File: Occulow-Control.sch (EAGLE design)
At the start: 39 parts, among them J1 CORTEX_DEBUG_PTH, T1 DMP3010LK3, T2 DMP3010LK3, T3 DMP3010LK3

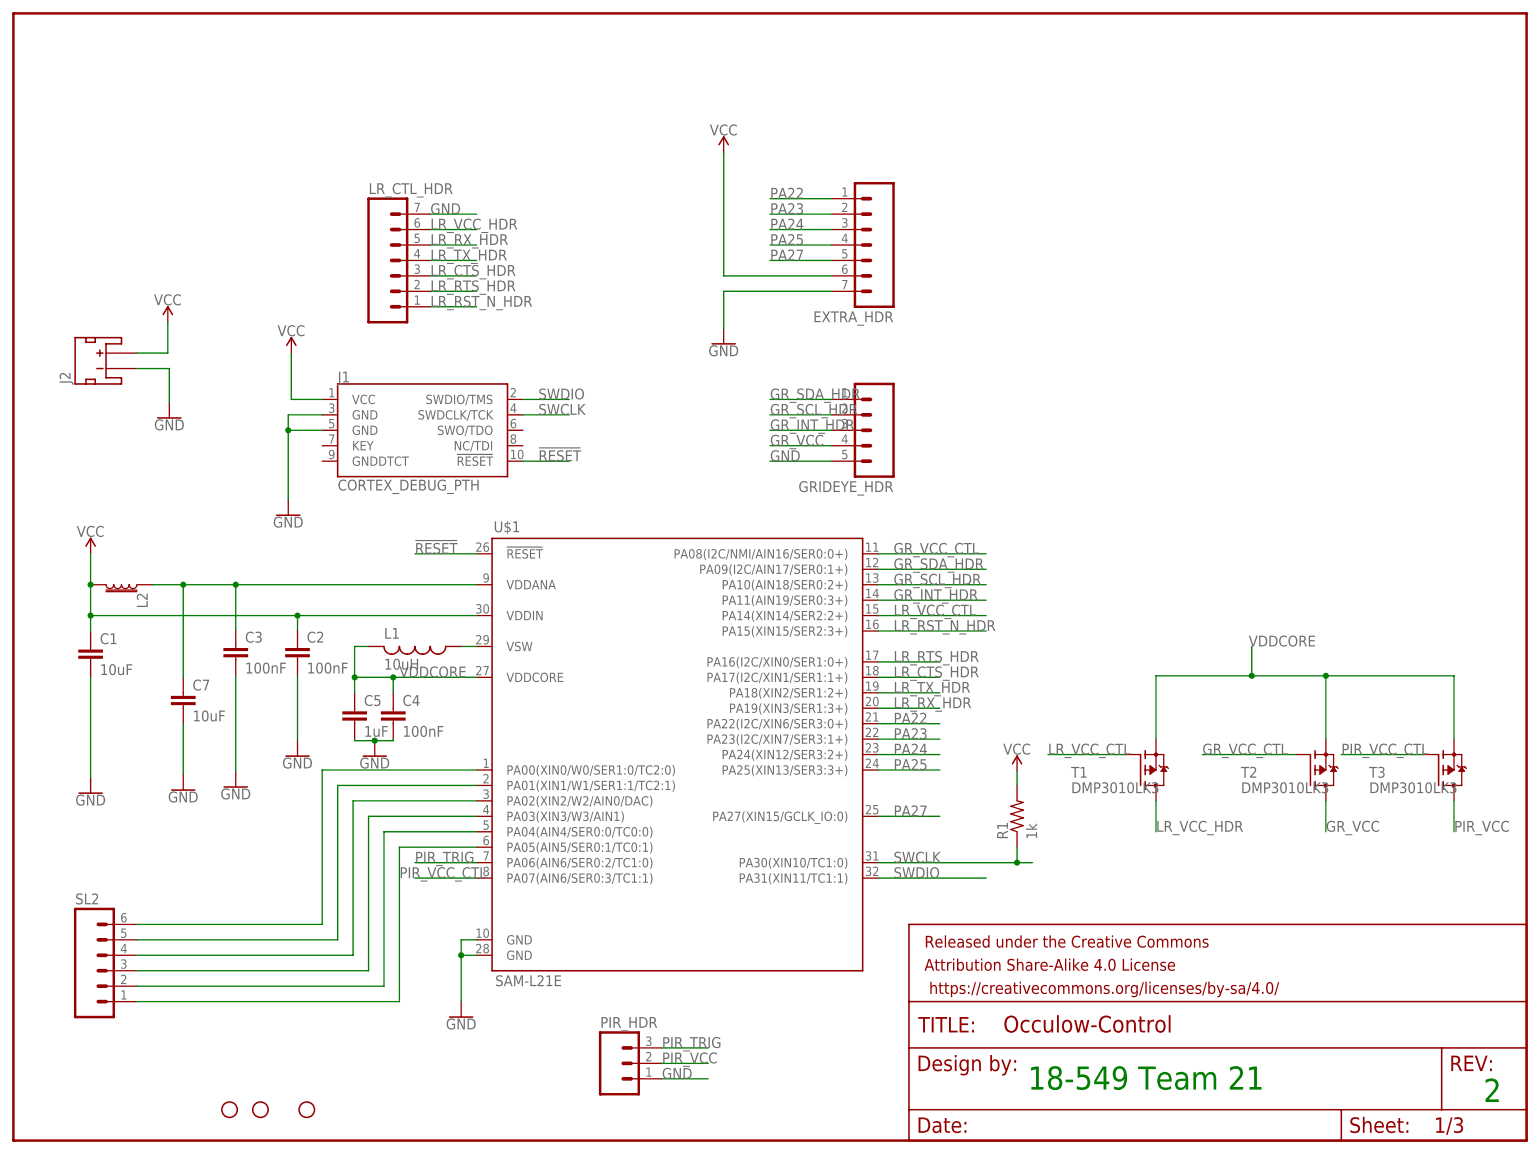
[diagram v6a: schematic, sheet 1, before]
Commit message: SAM portion fully routed
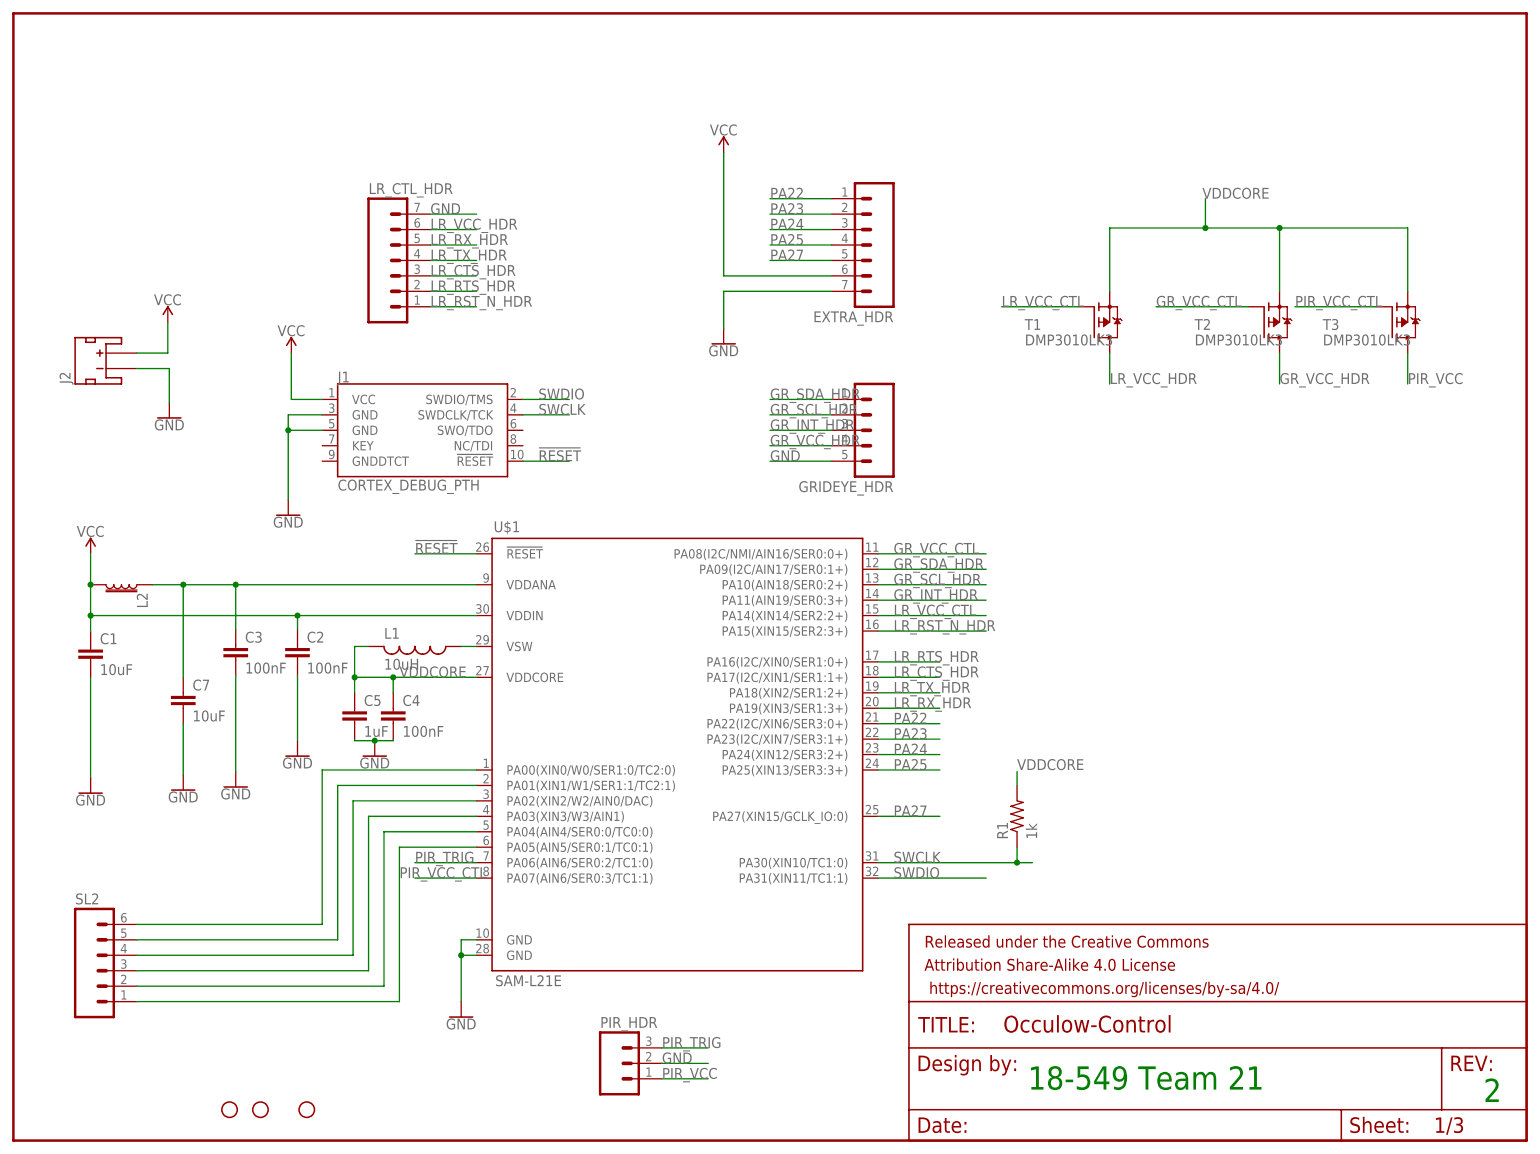
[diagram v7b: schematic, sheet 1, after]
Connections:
- new net GR_VCC_HDR: GRIDEYE_HDR.4, T2.D
- net GND: now also PIR_HDR.2; no longer PIR_HDR.1
- net GR_VCC: no longer GRIDEYE_HDR.4, T2.D
- net PIR_VCC: now also PIR_HDR.1; no longer PIR_HDR.2
- net VCC: no longer R1.2
- net VDDCORE: now also R1.2
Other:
- moved on the sheet: T1, T2, T3
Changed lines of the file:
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@@
 <part name="T3" library="transistor-fet" deviceset="SPD30P06P" device="TO252" value="DMP3010LK3"/>
 <part name="R1" library="resistor" deviceset="R-US_" device="R1206" value="1k"/>
-<part name="SUPPLY2" library="SparkFun-PowerSymbols" deviceset="VCC" device=""/>
 <part name="J1" library="SparkFun-Connectors" deviceset="CORTEX_DEBUG" device="_PTH"/>
 <part name="SUPPLY4" library="SparkFun-PowerSymbols" deviceset="VCC" device=""/>
@@
 <instance part="GND2" gate="1" x="12.7" y="57.15"/>
 <instance part="GND3" gate="1" x="36.576" y="58.166"/>
-<instance part="T1" gate="G$1" x="185.42" y="60.96"/>
+<instance part="T1" gate="G$1" x="177.8" y="134.62"/>
 <instance part="GRIDEYE_HDR" gate="G$1" x="142.24" y="116.84" rot="R180"/>
-<instance part="T2" gate="G$1" x="213.36" y="60.96"/>
+<instance part="T2" gate="G$1" x="205.74" y="134.62"/>
 <instance part="PIR_HDR" gate="G$1" x="99.06" y="12.7"/>
-<instance part="T3" gate="G$1" x="234.442" y="60.96"/>
+<instance part="T3" gate="G$1" x="226.822" y="134.62"/>
 <instance part="R1" gate="G$1" x="165.1" y="53.34" rot="R90"/>
-<instance part="SUPPLY2" gate="G$1" x="165.1" y="60.706"/>
 <instance part="J1" gate="G$1" x="66.04" y="116.84"/>
 <instance part="SUPPLY4" gate="G$1" x="45.72" y="129.54"/>
@@
 </segment>
 <segment>
-<pinref part="PIR_HDR" gate="G$1" pin="1"/>
-<wire x1="106.68" y1="10.16" x2="114.3" y2="10.16" width="0.1524" layer="91"/>
-<label x="106.68" y="10.16" size="1.778" layer="95"/>
+<pinref part="PIR_HDR" gate="G$1" pin="2"/>
+<wire x1="106.68" y1="12.7" x2="114.3" y2="12.7" width="0.1524" layer="91"/>
+<label x="106.68" y="12.7" size="1.778" layer="95"/>
 </segment>
 <segment>
@@
 </net>
 <net name="VCC" class="0">
-<segment>
-<pinref part="SUPPLY2" gate="G$1" pin="VCC"/>
-<pinref part="R1" gate="G$1" pin="2"/>
-<wire x1="165.1" y1="60.706" x2="165.1" y2="58.42" width="0.1524" layer="91"/>
-</segment>
 <segment>
 <pinref part="J1" gate="G$1" pin="VCC"/>
@@
 <segment>
 <pinref part="T1" gate="G$1" pin="G"/>
-<wire x1="182.88" y1="63.5" x2="170.18" y2="63.5" width="0.1524" layer="91"/>
-<label x="170.18" y="63.5" size="1.778" layer="95"/>
+<wire x1="175.26" y1="137.16" x2="162.56" y2="137.16" width="0.1524" layer="91"/>
+<label x="162.56" y="137.16" size="1.778" layer="95"/>
 </segment>
 <segment>
@@
 <segment>
 <pinref part="T2" gate="G$1" pin="G"/>
-<wire x1="210.82" y1="63.5" x2="195.58" y2="63.5" width="0.1524" layer="91"/>
-<label x="195.58" y="63.5" size="1.778" layer="95"/>
+<wire x1="203.2" y1="137.16" x2="187.96" y2="137.16" width="0.1524" layer="91"/>
+<label x="187.96" y="137.16" size="1.778" layer="95"/>
 </segment>
 <segment>
@@
 <wire x1="142.24" y1="96.52" x2="160.02" y2="96.52" width="0.1524" layer="91"/>
 <label x="144.78" y="96.52" size="1.778" layer="95"/>
-</segment>
-</net>
-<net name="GR_VCC" class="0">
-<segment>
-<pinref part="T2" gate="G$1" pin="D"/>
-<wire x1="215.9" y1="55.88" x2="215.9" y2="50.8" width="0.1524" layer="91"/>
-<label x="215.9" y="50.8" size="1.778" layer="95"/>
-</segment>
-<segment>
-<pinref part="GRIDEYE_HDR" gate="G$1" pin="4"/>
-<wire x1="134.62" y1="114.3" x2="124.46" y2="114.3" width="0.1524" layer="91"/>
-<label x="124.46" y="114.3" size="1.778" layer="95"/>
 </segment>
 </net>
@@
 <net name="PIR_VCC" class="0">
 <segment>
-<pinref part="PIR_HDR" gate="G$1" pin="2"/>
-<wire x1="106.68" y1="12.7" x2="114.3" y2="12.7" width="0.1524" layer="91"/>
-<label x="106.68" y="12.7" size="1.778" layer="95"/>
+<pinref part="PIR_HDR" gate="G$1" pin="1"/>
+<wire x1="106.68" y1="10.16" x2="114.3" y2="10.16" width="0.1524" layer="91"/>
+<label x="106.68" y="10.16" size="1.778" layer="95"/>
 </segment>
 <segment>
 <pinref part="T3" gate="G$1" pin="D"/>
-<wire x1="236.982" y1="55.88" x2="236.982" y2="50.8" width="0.1524" layer="91"/>
-<label x="236.982" y="50.8" size="1.778" layer="95"/>
+<wire x1="229.362" y1="129.54" x2="229.362" y2="124.46" width="0.1524" layer="91"/>
+<label x="229.362" y="124.46" size="1.778" layer="95"/>
 </segment>
 </net>
@@
 <segment>
 <pinref part="T3" gate="G$1" pin="G"/>
-<wire x1="231.902" y1="63.5" x2="218.44" y2="63.5" width="0.1524" layer="91"/>
-<label x="218.44" y="63.5" size="1.778" layer="95"/>
+<wire x1="224.282" y1="137.16" x2="210.82" y2="137.16" width="0.1524" layer="91"/>
+<label x="210.82" y="137.16" size="1.778" layer="95"/>
 </segment>
 <segment>
@@
 </segment>
 <segment>
-<wire x1="203.708" y1="81.28" x2="203.708" y2="76.454" width="0.1524" layer="91"/>
+<wire x1="196.088" y1="154.94" x2="196.088" y2="150.114" width="0.1524" layer="91"/>
 <pinref part="T1" gate="G$1" pin="S"/>
-<wire x1="203.708" y1="76.454" x2="187.96" y2="76.454" width="0.1524" layer="91"/>
-<wire x1="187.96" y1="76.454" x2="187.96" y2="66.04" width="0.1524" layer="91"/>
+<wire x1="196.088" y1="150.114" x2="180.34" y2="150.114" width="0.1524" layer="91"/>
+<wire x1="180.34" y1="150.114" x2="180.34" y2="139.7" width="0.1524" layer="91"/>
 <pinref part="T2" gate="G$1" pin="S"/>
-<wire x1="203.708" y1="76.454" x2="215.9" y2="76.454" width="0.1524" layer="91"/>
-<wire x1="215.9" y1="76.454" x2="215.9" y2="66.04" width="0.1524" layer="91"/>
-<junction x="203.708" y="76.454"/>
+<wire x1="196.088" y1="150.114" x2="208.28" y2="150.114" width="0.1524" layer="91"/>
+<wire x1="208.28" y1="150.114" x2="208.28" y2="139.7" width="0.1524" layer="91"/>
+<junction x="196.088" y="150.114"/>
 <pinref part="T3" gate="G$1" pin="S"/>
-<wire x1="215.9" y1="76.454" x2="236.982" y2="76.454" width="0.1524" layer="91"/>
-<wire x1="236.982" y1="76.454" x2="236.982" y2="66.04" width="0.1524" layer="91"/>
-<junction x="215.9" y="76.454"/>
-<label x="203.2" y="81.28" size="1.778" layer="95"/>
+<wire x1="208.28" y1="150.114" x2="229.362" y2="150.114" width="0.1524" layer="91"/>
+<wire x1="229.362" y1="150.114" x2="229.362" y2="139.7" width="0.1524" layer="91"/>
+<junction x="208.28" y="150.114"/>
+<label x="195.58" y="154.94" size="1.778" layer="95"/>
+</segment>
+<segment>
+<pinref part="R1" gate="G$1" pin="2"/>
+<wire x1="165.1" y1="60.706" x2="165.1" y2="58.42" width="0.1524" layer="91"/>
+<label x="165.1" y="60.96" size="1.778" layer="95"/>
 </segment>
 </net>
@@
 <segment>
 <pinref part="T1" gate="G$1" pin="D"/>
-<wire x1="187.96" y1="55.88" x2="187.96" y2="50.8" width="0.1524" layer="91"/>
-<label x="187.96" y="50.8" size="1.778" layer="95"/>
+<wire x1="180.34" y1="129.54" x2="180.34" y2="124.46" width="0.1524" layer="91"/>
+<label x="180.34" y="124.46" size="1.778" layer="95"/>
 </segment>
 <segment>
@@
 </segment>
 </net>
+<net name="GR_VCC_HDR" class="0">
+<segment>
+<pinref part="GRIDEYE_HDR" gate="G$1" pin="4"/>
+<wire x1="134.62" y1="114.3" x2="124.46" y2="114.3" width="0.1524" layer="91"/>
+<label x="124.46" y="114.3" size="1.778" layer="95"/>
+</segment>
+<segment>
+<pinref part="T2" gate="G$1" pin="D"/>
+<wire x1="208.28" y1="129.54" x2="208.28" y2="124.46" width="0.1524" layer="91"/>
+<label x="208.28" y="124.46" size="1.778" layer="95"/>
+</segment>
+</net>

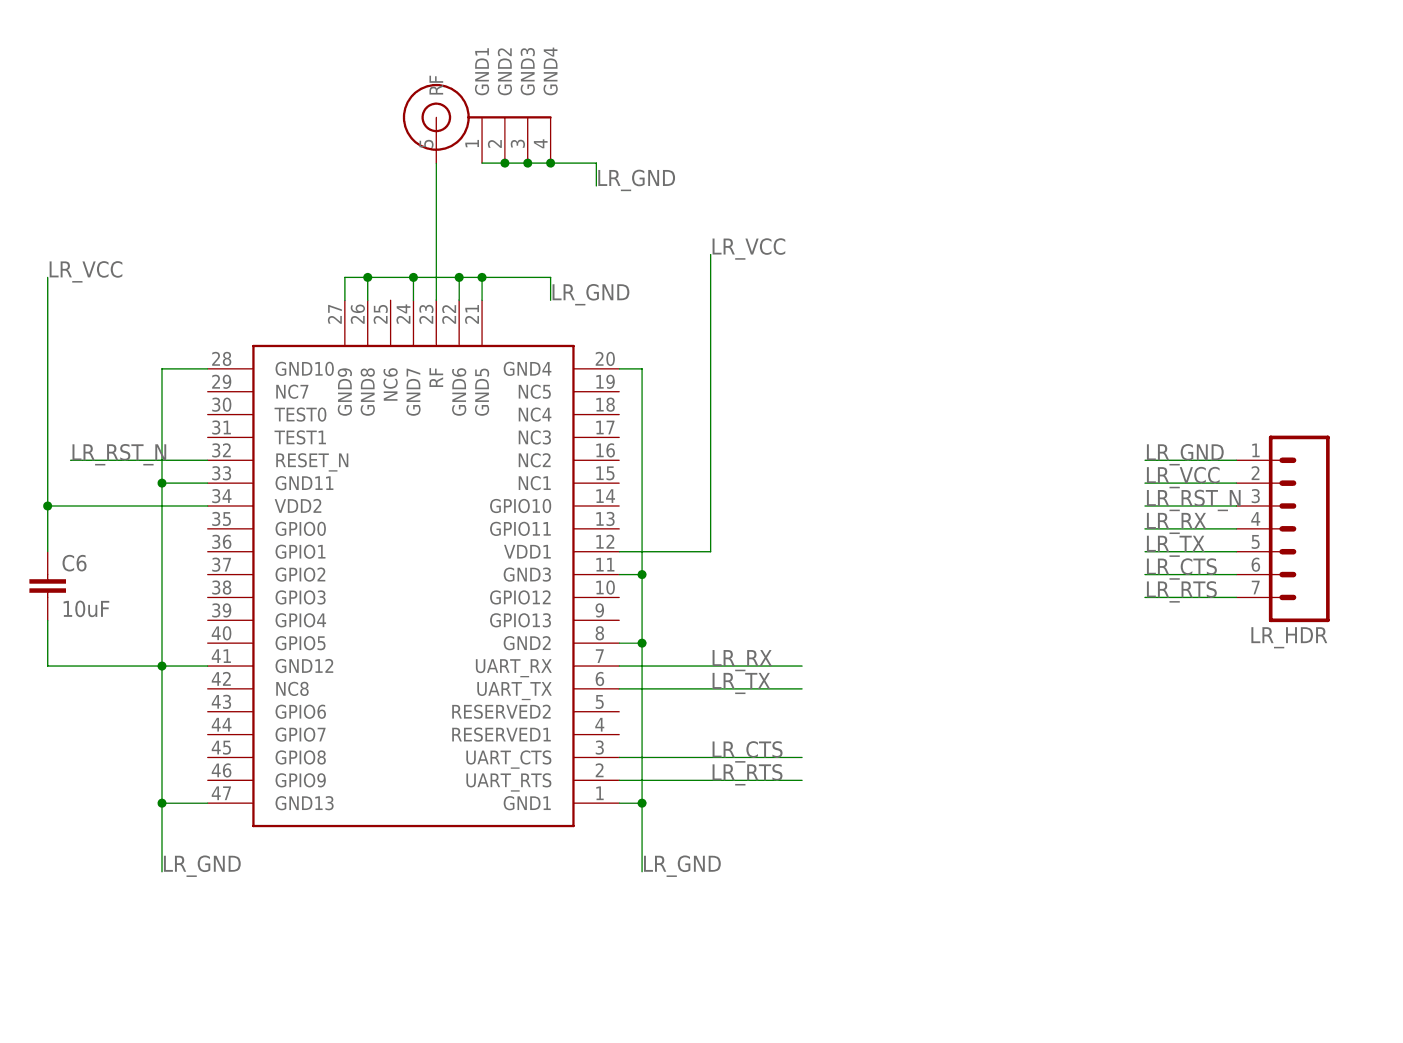
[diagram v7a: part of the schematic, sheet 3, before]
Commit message: Labels for most headers, moved some ground vias
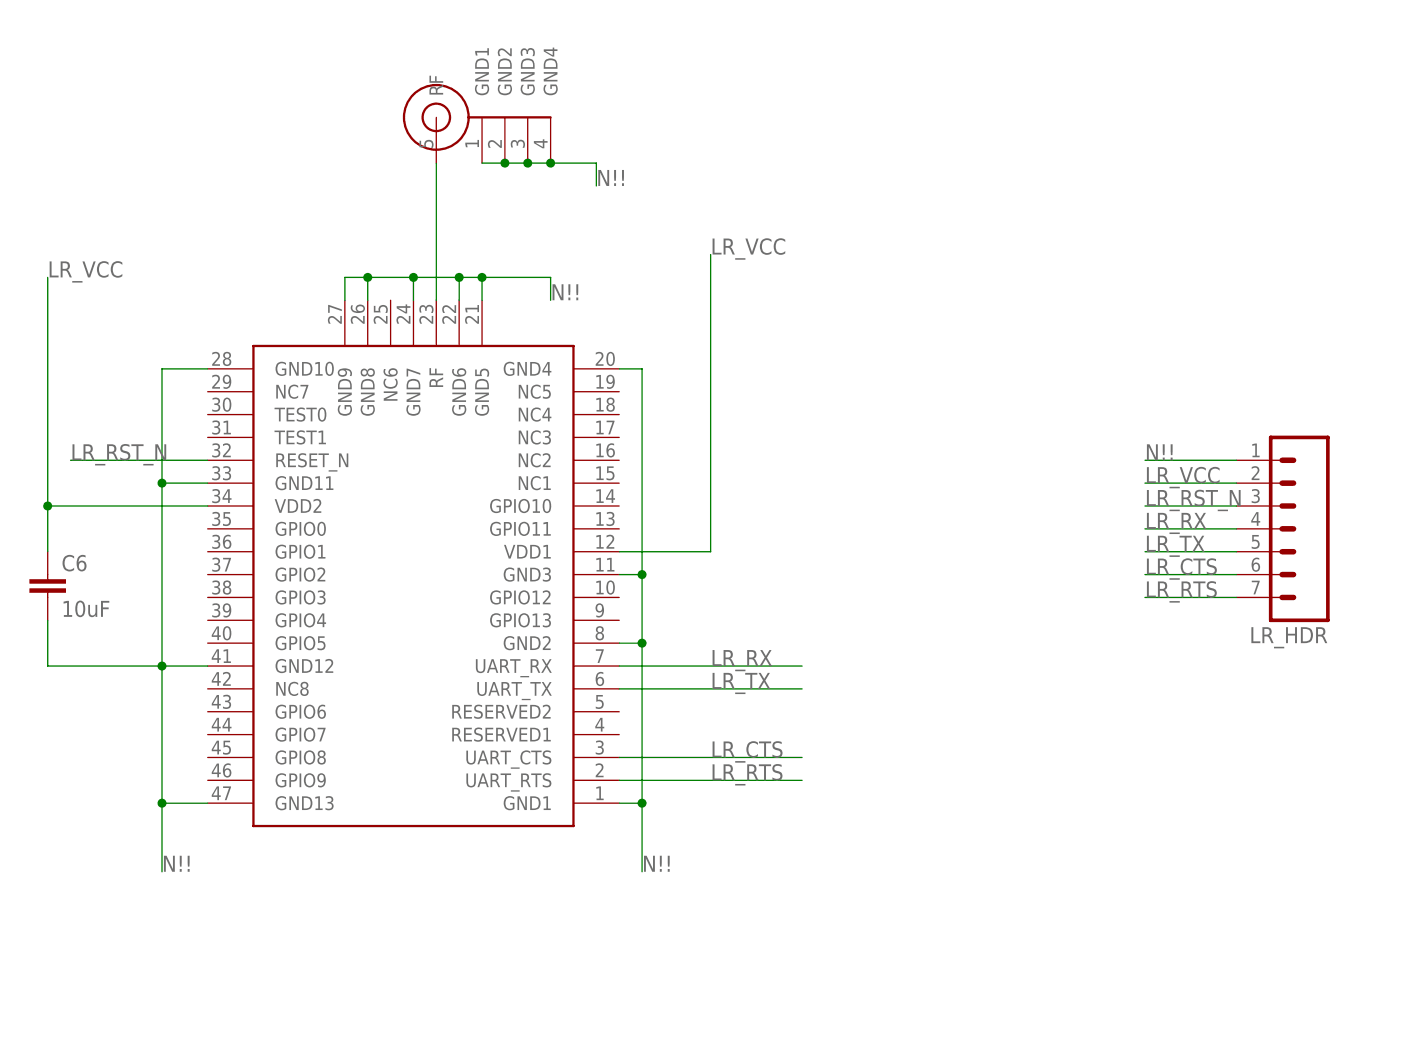
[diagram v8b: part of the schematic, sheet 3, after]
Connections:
- net LR_GND renamed N!!
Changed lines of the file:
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@@
 </segment>
 </net>
-<net name="LR_GND" class="0">
+<net name="N!!" class="0">
 <segment>
 <wire x1="63.5" y1="121.92" x2="63.5" y2="109.22" width="0.1524" layer="91"/>
